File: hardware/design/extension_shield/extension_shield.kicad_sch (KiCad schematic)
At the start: 10 parts

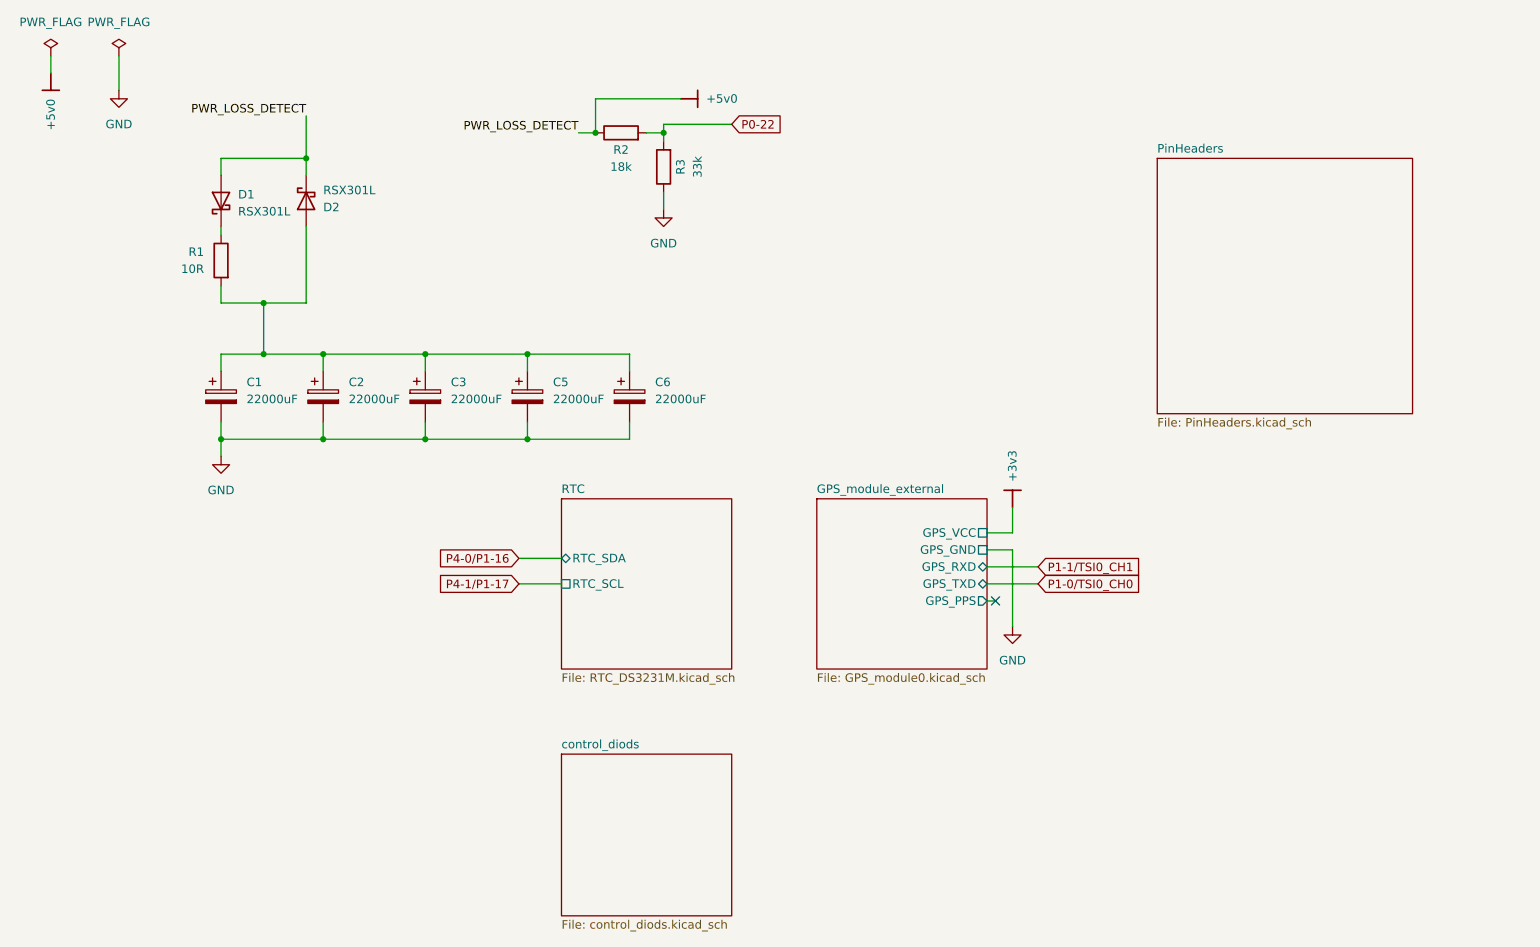
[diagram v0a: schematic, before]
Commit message: [HW/SHIELD] Adds Genereated PDF Schematic & Newer Version of Expansion Shield.
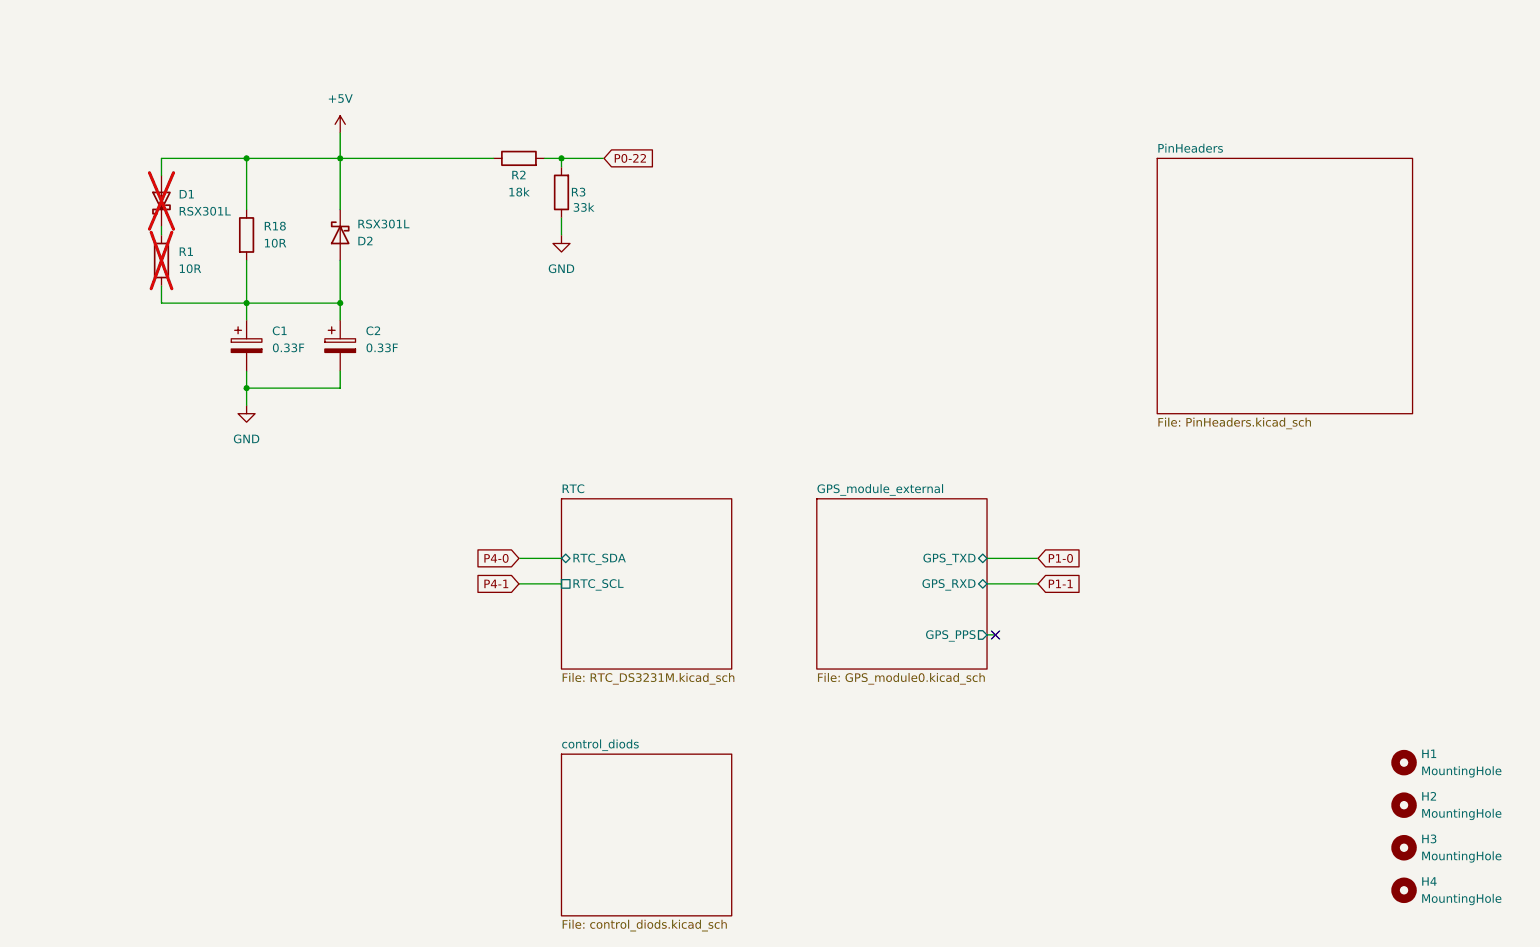
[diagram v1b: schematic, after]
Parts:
- removed C1, C2, C3, C5, C6: 22000uF, Capacitor_THT:CP_Radial_D18.0mm_P7.50mm, symbol Device:C_Polarized
- added C1, C2: 0.33F, SuperCapacitors:C_Radial_D8mm_W24mm_L14mm_P13.5mm, symbol SuperCapacitors:SCMR14G334SRBB0
- added H1, H2, H3, H4: MountingHole, MountingHole:MountingHole_3.2mm_M3, symbol Mechanical:MountingHole
- added R18: 10R, Resistor_THT:R_Axial_DIN0204_L3.6mm_D1.6mm_P5.08mm_Horizontal, symbol Device:R
- D1, R1: now not fitted
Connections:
- net GND: now also C1.2, C2.2
- net at D2.2 (A), R1.2: now also C1.1, C2.1, R18.2
- net +5v0 renamed +5V
- net +5V: now also R18.1
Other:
- sheet GPS_module_external ports: added none; removed GPS_GND, GPS_VCC
- title: (none) -> Datalogger Expansion Shield
- moved on the sheet: D2, R2, R3
